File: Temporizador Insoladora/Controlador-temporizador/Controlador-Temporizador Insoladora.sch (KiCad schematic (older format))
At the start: 76 parts, among them P1 ICSP, P2 VAC12V, P3 CARGA, P4 TRANSF, P5 VAC, P6 OPTO, P7 CONN_02X08, P8 OPTO, P9 OPTO, Q1 BC548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

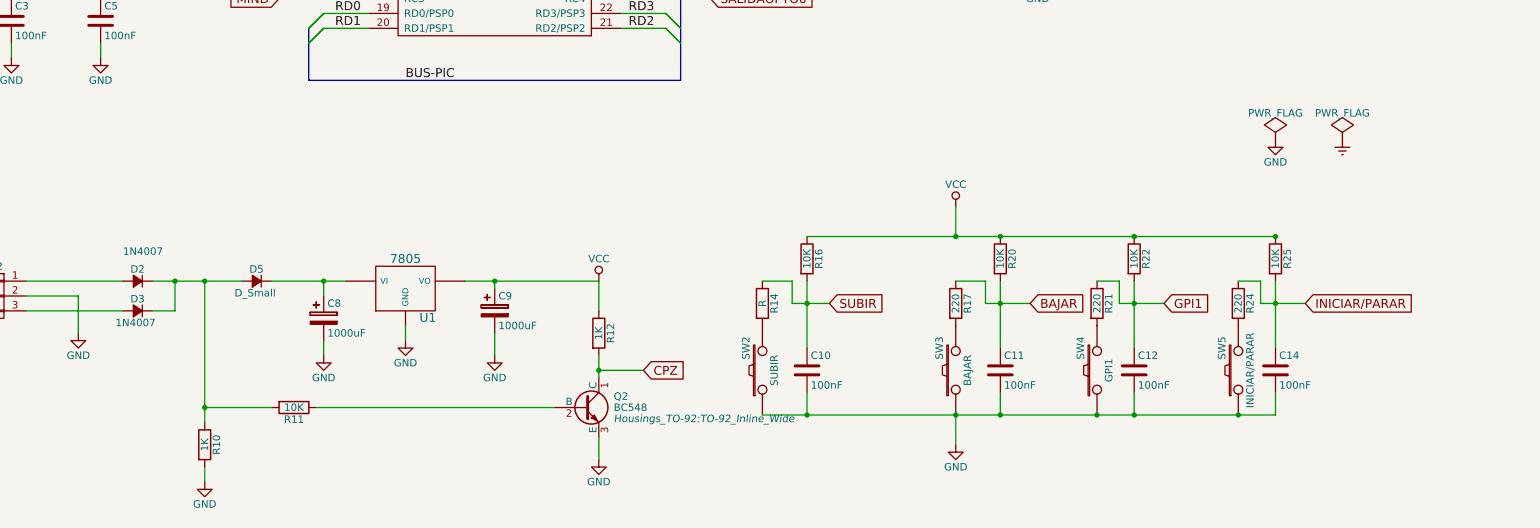
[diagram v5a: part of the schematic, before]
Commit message: Cambio del lugar donde se detecta el cruce por cero
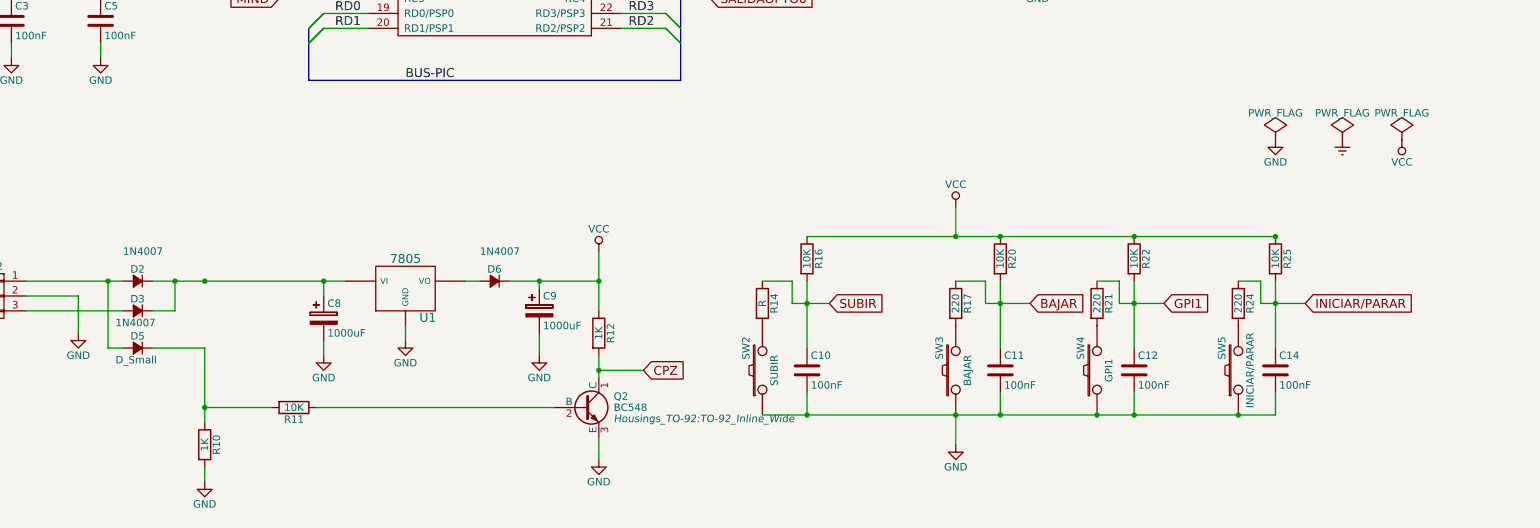
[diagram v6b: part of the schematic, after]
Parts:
- added D6: 1N4007, Diodes_ThroughHole:Diode_DO-41_SOD81_Horizontal_RM10, symbol D_Small
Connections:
- net VCC: now also D6.2 (C); no longer U1.VO
- net at D2.1 (A), P2.1 (P1): now also D5.1 (A)
- net at C8.1, U1.VI: now also D2.2 (C), D3.2 (C); no longer D5.2 (C)
- new net: D5.2 (C), R10.1, R11.2
- new net: D6.1 (A), U1.VO
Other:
- moved on the sheet: C9, D5
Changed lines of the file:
@@
 L D_Small D5
 U 1 1 552AA2A9
-P 3200 5650
-F 0 "D5" H 3150 5730 50  0000 L CNN
-F 1 "D_Small" H 3050 5570 50  0000 L CNN
-F 2 "Diodes_ThroughHole:Diode_DO-41_SOD81_Horizontal_RM10" V 3200 5650 60  0001 C CNN
-F 3 "" V 3200 5650 60  0000 C CNN
-	1    3200 5650
+P 2400 6100
+F 0 "D5" H 2350 6180 50  0000 L CNN
+F 1 "D_Small" H 2250 6020 50  0000 L CNN
+F 2 "Diodes_ThroughHole:Diode_DO-41_SOD81_Horizontal_RM10" V 2400 6100 60  0001 C CNN
+F 3 "" V 2400 6100 60  0000 C CNN
+	1    2400 6100
 	1    0    0    -1
 $EndComp
@@
 L CP C9
 U 1 1 552AAAAD
-P 4800 5850
-F 0 "C9" H 4825 5950 50  0000 L CNN
-F 1 "1000uF" H 4825 5750 50  0000 L CNN
-F 2 "Capacitors_ThroughHole:C_Radial_D10_L16_P5" H 4838 5700 30  0001 C CNN
-F 3 "" H 4800 5850 60  0000 C CNN
-	1    4800 5850
+P 5100 5850
+F 0 "C9" H 5125 5950 50  0000 L CNN
+F 1 "1000uF" H 5125 5750 50  0000 L CNN
+F 2 "Capacitors_ThroughHole:C_Radial_D10_L16_P5" H 5138 5700 30  0001 C CNN
+F 3 "" H 5100 5850 60  0000 C CNN
+	1    5100 5850
 	1    0    0    -1
 $EndComp
@@
 L GND #PWR016
 U 1 1 552AAB01
-P 4800 6150
-F 0 "#PWR016" H 4800 5900 50  0001 C CNN
-F 1 "GND" H 4800 6000 50  0000 C CNN
-F 2 "" H 4800 6150 60  0000 C CNN
-F 3 "" H 4800 6150 60  0000 C CNN
-	1    4800 6150
+P 5100 6150
+F 0 "#PWR016" H 5100 5900 50  0001 C CNN
+F 1 "GND" H 5100 6000 50  0000 C CNN
+F 2 "" H 5100 6150 60  0000 C CNN
+F 3 "" H 5100 6150 60  0000 C CNN
+	1    5100 6150
 	1    0    0    -1
 $EndComp
@@
 L VCC #PWR019
 U 1 1 552AB298
-P 5500 5650
-F 0 "#PWR019" H 5500 5500 50  0001 C CNN
-F 1 "VCC" H 5500 5800 50  0000 C CNN
-F 2 "" H 5500 5650 60  0000 C CNN
-F 3 "" H 5500 5650 60  0000 C CNN
-	1    5500 5650
+P 5500 5450
+F 0 "#PWR019" H 5500 5300 50  0001 C CNN
+F 1 "VCC" H 5500 5600 50  0000 C CNN
+F 2 "" H 5500 5450 60  0000 C CNN
+F 3 "" H 5500 5450 60  0000 C CNN
+	1    5500 5450
 	1    0    0    -1
 $EndComp
@@
 	2650 5850 2650 5650
 Wire Wire Line
-	2500 5650 3100 5650
+	2500 5650 3800 5650
 Connection ~ 2650 5650
 Wire Wire Line
 	3650 5650 3650 5750
 Wire Wire Line
-	3300 5650 3800 5650
-Wire Wire Line
 	3650 6150 3650 6050
 Wire Wire Line
 	5500 6850 5500 6700
-Wire Wire Line
-	2850 5650 2850 6600
 Connection ~ 2850 5650
 Wire Wire Line
@@
 	5500 6150 5500 6300
 Wire Wire Line
-	5500 5650 5500 5850
-Wire Wire Line
-	4800 6000 4800 6150
-Wire Wire Line
-	4800 5700 4800 5650
-Connection ~ 4800 5650
+	5500 5450 5500 5850
+Wire Wire Line
+	5100 6000 5100 6150
+Wire Wire Line
+	5100 5700 5100 5650
+Connection ~ 5100 5650
 Wire Wire Line
 	3600 6500 5200 6500
@@
 	1    0    0    -1
 $EndComp
-Wire Wire Line
-	1100 4600 1100 4700
 $Comp
 L FUSE F1
@@
 	11550 3400 14150 3400
 Wire Wire Line
-	4600 5650 5500 5650
-Wire Wire Line
 	4000 9850 4000 9750
 Wire Bus Line
@@
 Wire Wire Line
 	6250 3650 5650 3650
+Wire Wire Line
+	2850 6100 2850 6600
+Wire Wire Line
+	2850 6100 2500 6100
+Wire Wire Line
+	2300 6100 2200 6100
+Wire Wire Line
+	2200 6100 2200 5650
+Connection ~ 2200 5650
+$Comp
+L D_Small D6
+U 1 1 555AB148
+P 4800 5650
+F 0 "D6" H 4750 5730 50  0000 L CNN
+F 1 "1N4007" H 4700 5850 50  0000 L CNN
+F 2 "Diodes_ThroughHole:Diode_DO-41_SOD81_Horizontal_RM10" V 4800 5650 60  0001 C CNN
+F 3 "" V 4800 5650 60  0000 C CNN
+	1    4800 5650
+	1    0    0    -1
+$EndComp
+Connection ~ 5500 5650
+Wire Wire Line
+	4600 5650 4700 5650
+Wire Wire Line
+	4900 5650 5500 5650
+Wire Wire Line
+	1100 4600 1100 4700
+$Comp
+L PWR_FLAG #FLG040
+U 1 1 555AFA47
+P 10900 4700
+F 0 "#FLG040" H 10900 4795 50  0001 C CNN
+F 1 "PWR_FLAG" H 10900 4880 50  0000 C CNN
+F 2 "" H 10900 4700 60  0000 C CNN
+F 3 "" H 10900 4700 60  0000 C CNN
+	1    10900 4700
+	1    0    0    -1
+$EndComp
+$Comp
+L VCC #PWR041
+U 1 1 555AFAEC
+P 10900 4700
+F 0 "#PWR041" H 10900 4550 50  0001 C CNN
+F 1 "VCC" H 10900 4850 50  0000 C CNN
+F 2 "" H 10900 4700 60  0000 C CNN
+F 3 "" H 10900 4700 60  0000 C CNN
+	1    10900 4700
+	-1   0    0    1
+$EndComp
 $EndSCHEMATC

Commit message: Casi termonado controlador, ver si los componentes se ajustan
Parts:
- C13: value 39nF -> 10nF; footprint Capacitors_ThroughHole:C_Rect_L4_W2.5_P2.5 -> Capacitors_ThroughHole:C_Rect_L7_W2.5_P5
- F1: value 1A -> 3A
- R23: value 10 -> 39
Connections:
- net at F1.2: now also P5.3 (P3); no longer P5.1 (P1)
- net at P3.2 (P2), P4.2 (P2), VR1.2: now also P5.1 (P1); no longer P5.3 (P3)
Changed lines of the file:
@@
 P 12800 2550
 F 0 "R23" V 12880 2550 50  0000 C CNN
-F 1 "10" V 12800 2550 50  0000 C CNN
+F 1 "39" V 12800 2550 50  0000 C CNN
 F 2 "Discret:R3" V 12730 2550 30  0001 C CNN
 F 3 "" H 12800 2550 30  0000 C CNN
@@
 P 12800 3150
 F 0 "C13" H 12825 3250 50  0000 L CNN
-F 1 "39nF" H 12825 3050 50  0000 L CNN
-F 2 "Capacitors_ThroughHole:C_Rect_L4_W2.5_P2.5" H 12838 3000 30  0001 C CNN
+F 1 "10nF" H 12825 3050 50  0000 L CNN
+F 2 "Capacitors_ThroughHole:C_Rect_L7_W2.5_P5" H 12838 3000 30  0001 C CNN
 F 3 "" H 12800 3150 60  0000 C CNN
 	1    12800 3150
@@
 P 13500 2850
 F 0 "F1" H 13600 2900 50  0000 C CNN
-F 1 "1A" H 13400 2800 50  0000 C CNN
+F 1 "3A" H 13400 2800 50  0000 C CNN
 F 2 "Fuse_Holders_and_Fuses:Fuseholder5x20_horiz_open_lateral_Type-II" H 13500 2850 60  0001 C CNN
 F 3 "" H 13500 2850 60  0000 C CNN
@@
 F 3 "" H 14400 2950 60  0000 C CNN
 	1    14400 2950
-	1    0    0    -1
+	1    0    0    1
 $EndComp
 $Comp

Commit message: Controlador finalizado
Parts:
- added P10: CONN_01X08, Socket_Strips:Socket_Strip_Straight_1x08, symbol CONN_01X08
- R14: value R -> 220
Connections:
- net GND: now also P10.2 (P2), P10.4 (P4), P10.6 (P6), P10.8 (P8)
- net at R21.2, SW4.2: now also P10.7 (P7)
- net at R14.2, SW2.2: now also P10.1 (P1)
- net at R17.2, SW3.2: now also P10.3 (P3)
- net at R24.2, SW5.2: now also P10.5 (P5)
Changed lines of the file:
@@
 L GND #PWR026
 U 1 1 552B01E5
-P 7900 6750
-F 0 "#PWR026" H 7900 6500 50  0001 C CNN
-F 1 "GND" H 7900 6600 50  0000 C CNN
-F 2 "" H 7900 6750 60  0000 C CNN
-F 3 "" H 7900 6750 60  0000 C CNN
-	1    7900 6750
+P 7900 6600
+F 0 "#PWR026" H 7900 6350 50  0001 C CNN
+F 1 "GND" H 7900 6450 50  0000 C CNN
+F 2 "" H 7900 6600 60  0000 C CNN
+F 3 "" H 7900 6600 60  0000 C CNN
+	1    7900 6600
 	1    0    0    -1
 $EndComp
@@
 	6600 6550 10050 6550
 Wire Wire Line
-	7900 6750 7900 6550
+	7900 6600 7900 6550
 Connection ~ 7900 6550
 $Comp
@@
 P 6600 5800
 F 0 "R14" V 6680 5800 50  0000 C CNN
-F 1 "R" V 6600 5800 50  0000 C CNN
+F 1 "220" V 6600 5800 50  0000 C CNN
 F 2 "Discret:R3" V 6530 5800 30  0001 C CNN
 F 3 "" H 6600 5800 30  0000 C CNN
@@
 	-1   0    0    1
 $EndComp
+$Comp
+L CONN_01X08 P10
+U 1 1 555D0F48
+P 8100 7400
+F 0 "P10" H 8100 7850 50  0000 C CNN
+F 1 "CONN_01X08" V 8200 7400 50  0000 C CNN
+F 2 "Socket_Strips:Socket_Strip_Straight_1x08" H 8100 7400 60  0001 C CNN
+F 3 "" H 8100 7400 60  0000 C CNN
+	1    8100 7400
+	0    -1   1    0
+$EndComp
+Wire Wire Line
+	7750 7200 7750 6950
+Wire Wire Line
+	7750 6950 6400 6950
+Wire Wire Line
+	6400 6950 6400 5950
+Wire Wire Line
+	6400 5950 6600 5950
+Wire Wire Line
+	7850 7200 7850 7000
+Wire Wire Line
+	7850 7000 8450 7000
+Wire Wire Line
+	8050 6550 8050 7200
+Wire Wire Line
+	8250 7000 8250 7200
+Connection ~ 8050 7000
+Wire Wire Line
+	8450 7000 8450 7200
+Connection ~ 8250 7000
+Wire Wire Line
+	9600 6950 9600 5950
+Wire Wire Line
+	9600 5950 9800 5950
+Wire Wire Line
+	8650 6900 8650 5950
+Wire Wire Line
+	8650 5950 8850 5950
+Wire Wire Line
+	7950 7200 7950 6900
+Wire Wire Line
+	7950 6900 7550 6900
+Wire Wire Line
+	7550 6900 7550 5950
+Wire Wire Line
+	7550 5950 7900 5950
+Connection ~ 8050 6550
+Wire Wire Line
+	8650 6900 8350 6900
+Wire Wire Line
+	8350 6900 8350 7200
+Wire Wire Line
+	9600 6950 8150 6950
+Wire Wire Line
+	8150 6950 8150 7200
 $EndSCHEMATC
